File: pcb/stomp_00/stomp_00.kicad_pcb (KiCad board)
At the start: 2 copper layers, 50 x 60 mm, 21 parts, among them J1 9V_Power_Input, J5 Conn_01x08_Pin, J6 Conn_01x08_Pin, J7 Conn_01x08_Pin, U4 XL1509-5.0, U5 AP7333-33SRG, U6 74HC595, U7 74HC165, U8 74HC4051, U9 SGTL5000XNAA3

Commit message: taking shape...
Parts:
- moved H1 81.6 mm to (87.0, -24.0)
- moved H2 81.6 mm to (117.0, -24.0)
- moved H3 81.6 mm to (80.0, 30.0)
- moved H4 81.6 mm to (124.0, 30.0)
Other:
- board size 50 x 60 mm -> 56 x 65 mm
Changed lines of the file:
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@@
   )
   (footprint "MountingHole:MountingHole_3.2mm_M3" (layer "F.Cu")
-    (at 3 57)
+    (at 80 30)
     (descr "Mounting Hole 3.2mm, no annular, M3")
     (tags "mounting hole 3.2mm no annular m3")
@@
   )
   (footprint "MountingHole:MountingHole_3.2mm_M3" (layer "F.Cu")
-    (at 40 3)
+    (at 117 -24)
     (descr "Mounting Hole 3.2mm, no annular, M3")
     (tags "mounting hole 3.2mm no annular m3")
@@
   )
   (footprint "MountingHole:MountingHole_3.2mm_M3" (layer "F.Cu")
-    (at 47 57)
+    (at 124 30)
     (descr "Mounting Hole 3.2mm, no annular, M3")
     (tags "mounting hole 3.2mm no annular m3")
@@
   )
   (footprint "MountingHole:MountingHole_3.2mm_M3" (layer "F.Cu")
-    (at 10 3)
+    (at 87 -24)
     (descr "Mounting Hole 3.2mm, no annular, M3")
     (tags "mounting hole 3.2mm no annular m3")
@@
     )
   )
-  (gr_rect (start 16 22) (end 34 60)
-    (stroke (width 0.15) (type default)) (fill none) (layer "Dwgs.User"))
-  (gr_rect (start 0 35) (end 50 60)
-    (stroke (width 0.15) (type default)) (fill none) (layer "Dwgs.User"))
-  (gr_line (start 50 8) (end 50 60)
+  (gr_line (start 56 8) (end 56 65)
     (stroke (width 0.1) (type default)) (layer "Edge.Cuts"))
-  (gr_line (start 50 60) (end 0 60)
+  (gr_line (start 56 65) (end 0 65)
     (stroke (width 0.1) (type default)) (layer "Edge.Cuts"))
-  (gr_line (start 8 0) (end 42 0)
+  (gr_line (start 8 0) (end 48 0)
     (stroke (width 0.1) (type default)) (layer "Edge.Cuts"))
   (gr_arc (start 8 0) (mid 5.656854 5.656854) (end 0 8)
     (stroke (width 0.1) (type default)) (layer "Edge.Cuts"))
-  (gr_line (start 0 60) (end 0 8)
+  (gr_line (start 0 65) (end 0 8)
     (stroke (width 0.1) (type default)) (layer "Edge.Cuts"))
-  (gr_arc (start 50 8) (mid 44.343146 5.656854) (end 42 0)
+  (gr_arc (start 56 8) (mid 50.343146 5.656854) (end 48 0)
     (stroke (width 0.1) (type default)) (layer "Edge.Cuts"))
 )

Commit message: teensy footprint
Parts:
- removed U8: 74HC4051, Package_SO:SOIC-16_3.9x9.9mm_P1.27mm
- added D3: 1N4148, Diode_SMD:D_SOD-123, F.Cu at (194.2, 68.7)
- added J10: AudioJack3, Connector_PinHeader_2.54mm:PinHeader_1x03_P2.54mm_Vertical, F.Cu at (184.3, 69.4)
- added J11: AudioJack3, Connector_PinHeader_2.54mm:PinHeader_1x03_P2.54mm_Vertical, F.Cu at (188.9, 69.4)
- added R1: 2.2k, Resistor_SMD:R_0603_1608Metric, F.Cu at (201.0, 73.5)
- added R10: R_US, Resistor_SMD:R_0603_1608Metric, F.Cu at (198.8, 44.2)
- added R11: R_US, Resistor_SMD:R_0603_1608Metric, F.Cu at (198.8, 46.7)
- added R17: 220R, Resistor_SMD:R_0603_1608Metric, F.Cu at (179.9, 56.6)
- added R18: 10k, Resistor_SMD:R_0603_1608Metric, F.Cu at (179.9, 59.1)
- added R19: 47R, Resistor_SMD:R_0603_1608Metric, F.Cu at (179.9, 61.6)
- added R2: 2.2k, Resistor_SMD:R_0603_1608Metric, F.Cu at (201.0, 76.0)
- added R20: 47R, Resistor_SMD:R_0603_1608Metric, F.Cu at (179.9, 64.1)
- added R21: 470R, Resistor_SMD:R_0603_1608Metric, F.Cu at (179.9, 66.6)
- added R3: 100, Resistor_SMD:R_0603_1608Metric, F.Cu at (201.0, 78.5)
- added R4: R_US, Resistor_SMD:R_0603_1608Metric, F.Cu at (198.8, 29.1)
- added R5: R_US, Resistor_SMD:R_0603_1608Metric, F.Cu at (198.8, 31.6)
- added R6: R_US, Resistor_SMD:R_0603_1608Metric, F.Cu at (198.8, 34.1)
- added R7: R_US, Resistor_SMD:R_0603_1608Metric, F.Cu at (198.8, 36.6)
- added R8: R_US, Resistor_SMD:R_0603_1608Metric, F.Cu at (198.8, 39.1)
- added R9: R_US, Resistor_SMD:R_0603_1608Metric, F.Cu at (198.8, 41.6)
- added RV1: R_Potentiometer_US, Potentiometer_THT:Potentiometer_Piher_PC-16_Single_Vertical, F.Cu at (14.9, 28.6)
- added RV2: R_Potentiometer_US, Potentiometer_THT:Potentiometer_Piher_PC-16_Single_Vertical, F.Cu at (32.5, 28.6)
- added RV3: R_Potentiometer_US, Potentiometer_THT:Potentiometer_Piher_PC-16_Single_Vertical, F.Cu at (50.0, 28.6)
- added SW1: SW_DIP_x04, Button_Switch_THT:SW_DIP_SPSTx04_Slide_9.78x12.34mm_W7.62mm_P2.54mm, F.Cu at (179.9, 42.5)
- added U1: 4051, Package_SO:SOIC-16_3.9x9.9mm_P1.27mm, F.Cu at (163.3, 33.6)
- added U11: 74HC165, Package_SO:SOIC-16_3.9x9.9mm_P1.27mm, F.Cu at (182.2, 33.6)
- added U12: 74HC595, Package_SO:SOIC-16_3.9x9.9mm_P1.27mm, F.Cu at (205.1, 33.6)
- added U13: 74HC165, Package_SO:SOIC-16_3.9x9.9mm_P1.27mm, F.Cu at (190.6, 33.6)
- added U14: 6N138, Package_DIP:PowerIntegrations_SMD-8, F.Cu at (188.0, 61.2)
- added U2: TL072, Package_SO:SOIC-8_3.9x4.9mm_P1.27mm, F.Cu at (203.3, 58.6)
- added U3: TL072, Package_SO:SOIC-8_3.9x4.9mm_P1.27mm, F.Cu at (203.3, 67.0)
- U6: value 74HC595 -> 4051
- U7: value 74HC165 -> Teensy4.1; footprint Package_SO:SOIC-16_3.9x9.9mm_P1.27mm -> teensy:Teensy41; moved to B.Cu
- moved J5 94.1 mm to (94.0, -5.62)
- moved U6 79.0 mm to (171.7, 33.6)
- moved U7 76.9 mm to (28.2, 32.2), turned to -90 degrees
- moved J7 75.8 mm to (81.0, 3.12)
- moved J6 49.0 mm to (97.0, 14.9)

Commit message: seeing whether everything will fit...
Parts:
- removed J7: Conn_01x08_Pin, Connector_PinHeader_2.54mm:PinHeader_1x08_P2.54mm_Vertical
- removed R10, R11, R4, R5, R6, R7, R8, R9: R_US, Resistor_SMD:R_0603_1608Metric
- removed RV1, RV2, RV3: R_Potentiometer_US, Potentiometer_THT:Potentiometer_Piher_PC-16_Single_Vertical
- removed U1, U6: 4051, Package_SO:SOIC-16_3.9x9.9mm_P1.27mm
- removed U11, U13: 74HC165, Package_SO:SOIC-16_3.9x9.9mm_P1.27mm
- removed U12: 74HC595, Package_SO:SOIC-16_3.9x9.9mm_P1.27mm
- added J4: Headphones, Connector_PinHeader_2.54mm:PinHeader_1x03_P2.54mm_Vertical, F.Cu at (90.2, 19.1)
- added J9: Conn_01x04_Pin, Connector_PinHeader_2.54mm:PinHeader_1x04_P2.54mm_Vertical, F.Cu at (167.8, 5.53)
- added RV4: R_Potentiometer_US, Potentiometer_THT:Potentiometer_Piher_PC-16_Single_Vertical, F.Cu at (15.6, 29.0)
- added RV5: R_Potentiometer_US, Potentiometer_THT:Potentiometer_Piher_PC-16_Single_Vertical, F.Cu at (33.2, 29.0)
- added RV6: R_Potentiometer_US, Potentiometer_THT:Potentiometer_Piher_PC-16_Single_Vertical, F.Cu at (50.7, 29.0)
- J1: footprint Connector_BarrelJack:BarrelJack_Horizontal -> Connector_PinHeader_2.54mm:PinHeader_1x03_P2.54mm_Vertical
- J5, J6: value Conn_01x08_Pin -> Conn_01x24_Pin; footprint Connector_PinHeader_2.54mm:PinHeader_1x08_P2.54mm_Vertical -> Connector_PinHeader_2.54mm:PinHeader_1x24_P2.54mm_Vertical
- SW1: moved to B.Cu
- moved SW1 131.9 mm to (50.8, 15.2), turned to 180 degrees
- moved C3 99.8 mm to (3.81, 58.4)
- moved J1 97.5 mm to (8.89, 7.62), turned to 90 degrees
- moved L1 96.7 mm to (3.81, 35.6)
- moved C5 85.0 mm to (3.81, 45.7)
- moved J5 76.8 mm to (17.8, 3.81)
- moved D2 72.7 mm to (12.7, 52.1), turned to 90 degrees
- moved J6 59.9 mm to (38.1, 3.81)
- moved U7 0.82 mm to (27.9, 33.0)
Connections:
- U7 pad 10: unconnected-(U7-8_TX2_IN1-Pad10) -> DAC_DOUT
- U7 pad 2: unconnected-(U7-0_RX1_CRX2_CS1-Pad2) -> MIDI_IN
- U7 pad 3: unconnected-(U7-1_TX1_CTX2_MISO1-Pad3) -> MIDI_OUT
- U7 pad 40: unconnected-(U7-18_A4_SDA-Pad40) -> DAC_SDA
- U7 pad 41: unconnected-(U7-19_A5_SCL-Pad41) -> DAC_SCL
- U7 pad 42: unconnected-(U7-20_A6_TX5_LRCLK1-Pad42) -> DAC_LRCLK
- U7 pad 43: unconnected-(U7-21_A7_RX5_BCLK1-Pad43) -> DAC_BCLK
- U7 pad 45: unconnected-(U7-23_A9_CRX1_MCLK1-Pad45) -> DAC_MCLK
- U7 pad 9: unconnected-(U7-7_RX2_OUT1A-Pad9) -> DAC_DIN

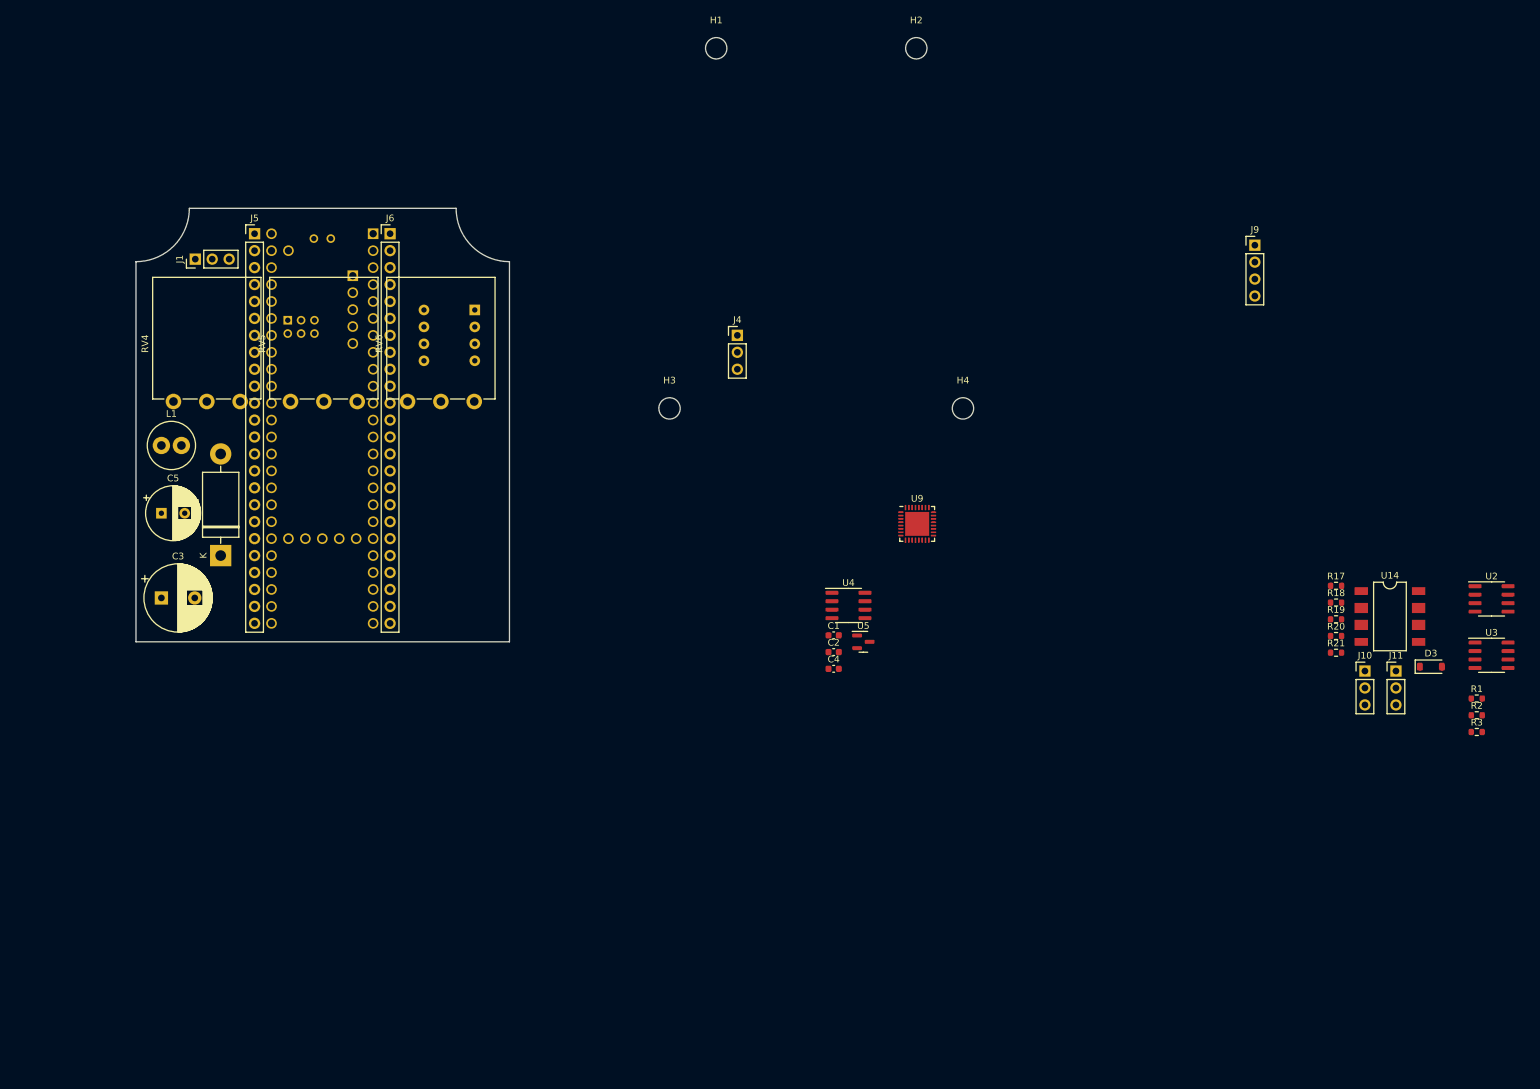
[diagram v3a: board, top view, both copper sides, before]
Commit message: input stage schematic
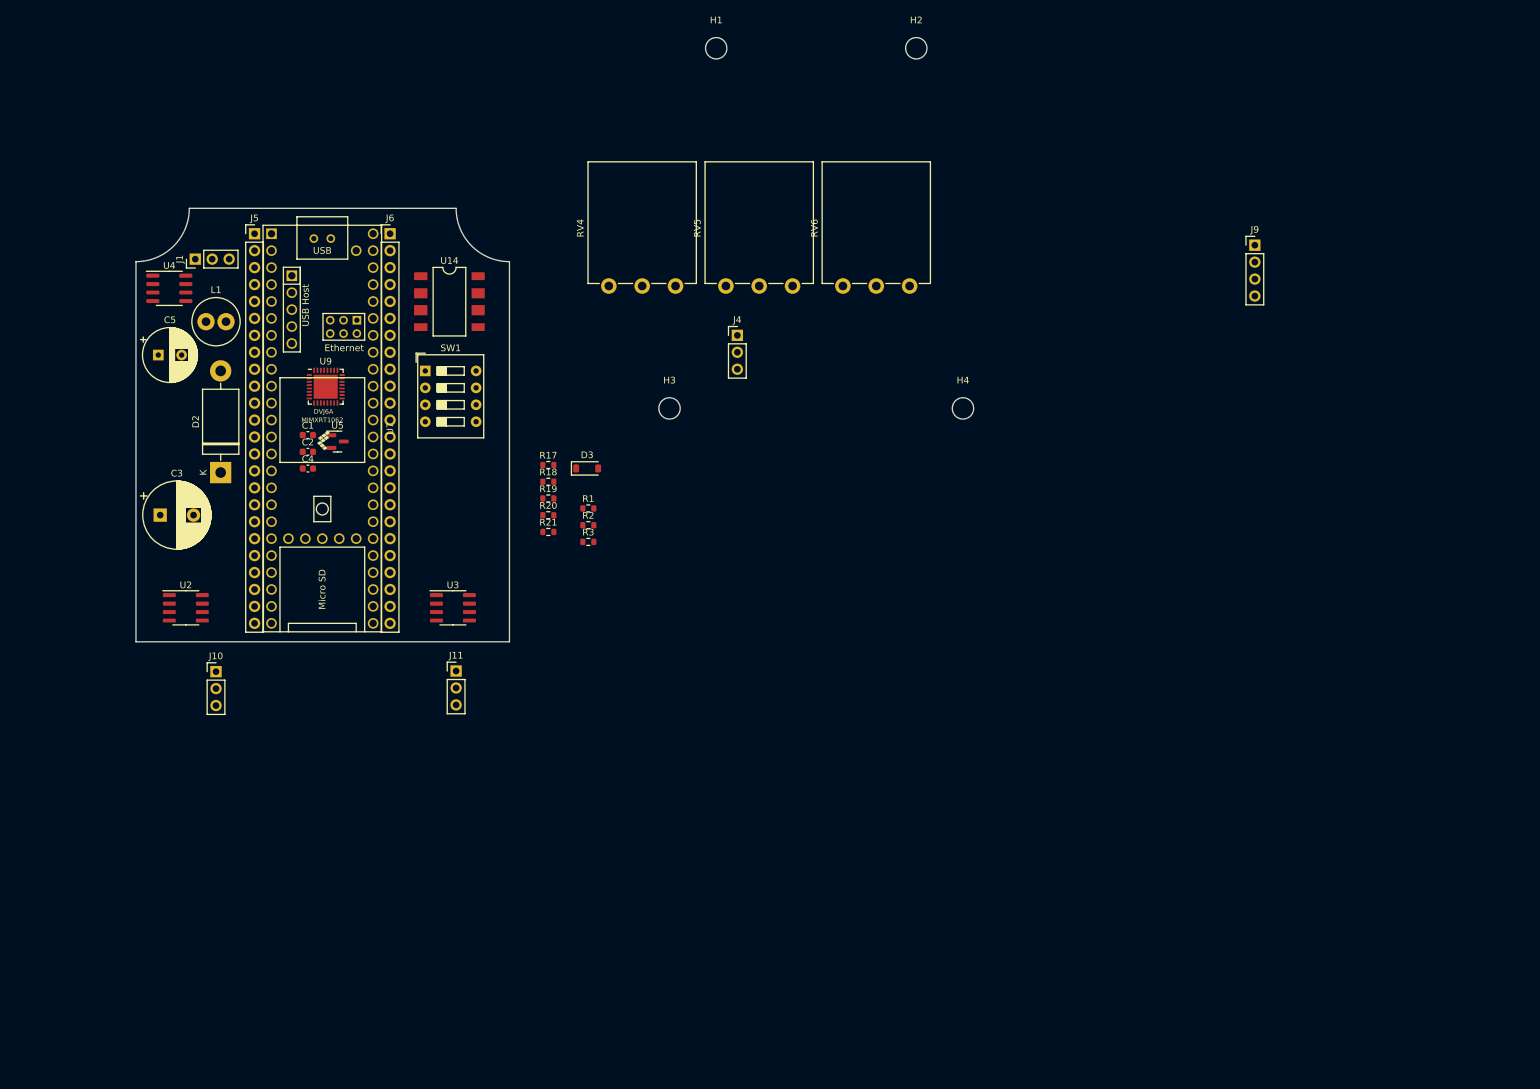
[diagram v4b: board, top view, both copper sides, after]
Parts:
- SW1, U7: moved to F.Cu
- moved U2 195.8 mm to (7.47, 59.9)
- moved J10 172.3 mm to (12.0, 69.5)
- moved U3 155.9 mm to (47.5, 59.9)
- moved U14 148.7 mm to (47.0, 14.0)
- moved J11 140.9 mm to (48.0, 69.4)
- moved R1 136.2 mm to (67.8, 45.0)
- moved R2 136.2 mm to (67.8, 47.5)
- moved R3 136.2 mm to (67.8, 50.0)
- moved D3 130.0 mm to (67.7, 39.0)
- moved R17 119.5 mm to (61.8, 38.5)
- moved R18 119.5 mm to (61.8, 41.0)
- moved R19 119.5 mm to (61.8, 43.5)
- moved R20 119.5 mm to (61.8, 46.0)
- moved R21 119.5 mm to (61.8, 48.5)
- moved U4 112.4 mm to (5.00, 12.0)
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
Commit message: better layout in enclosure
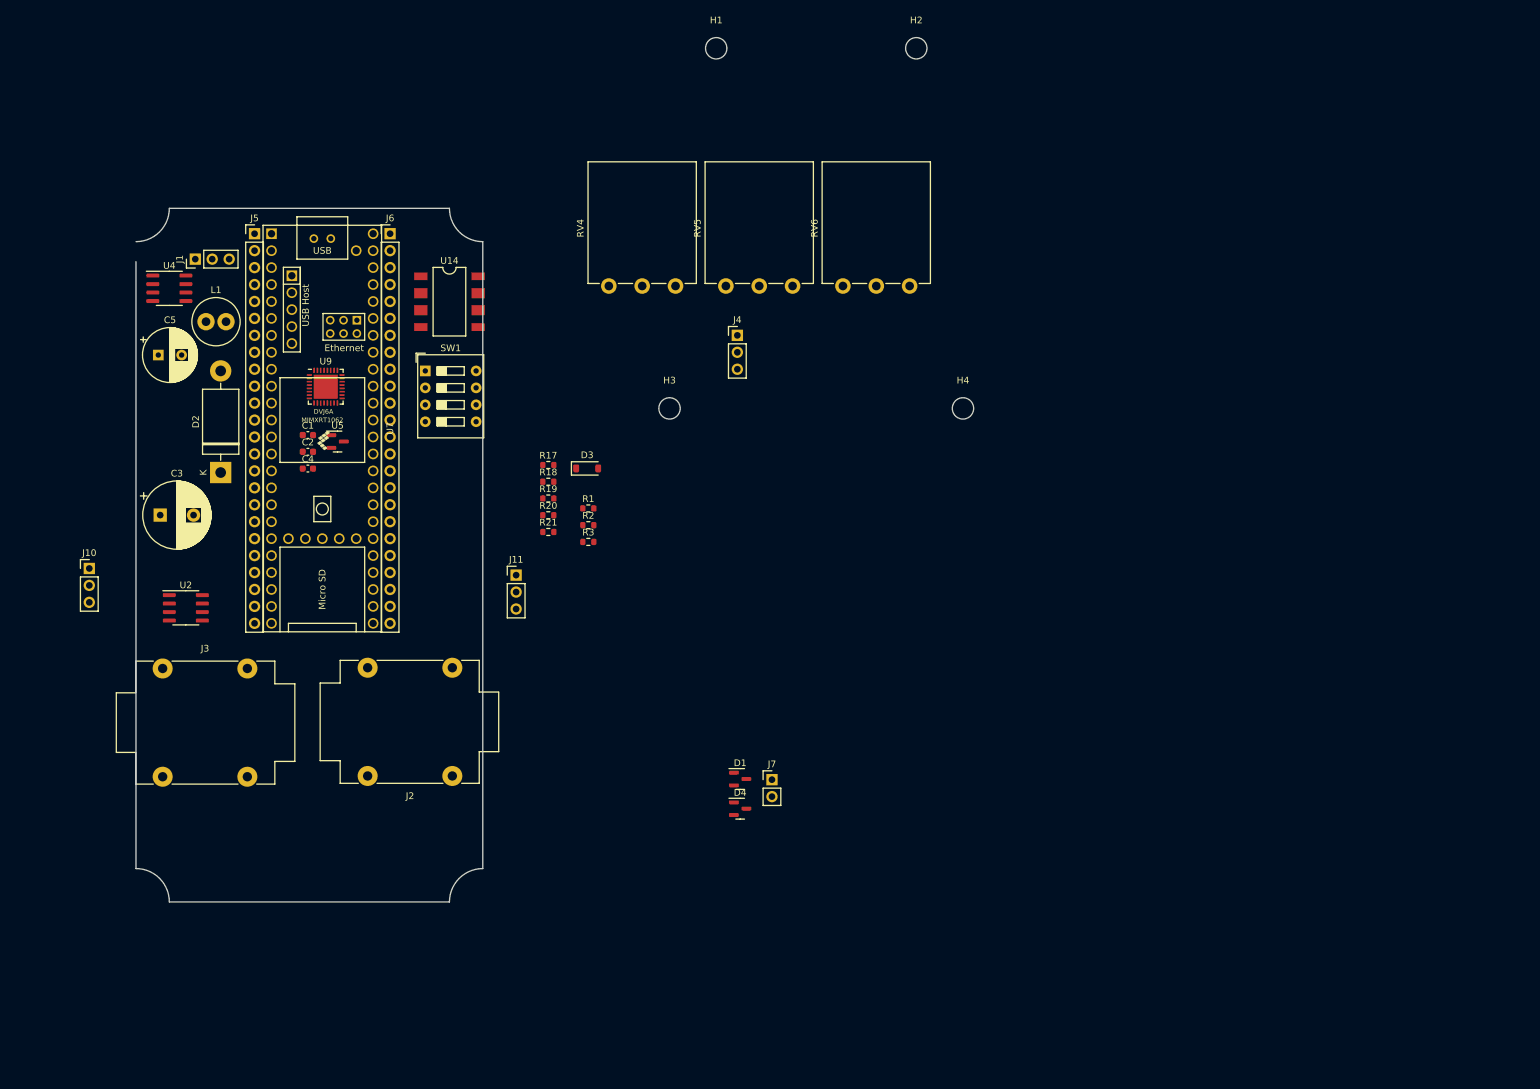
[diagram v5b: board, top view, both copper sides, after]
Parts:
- removed J9: Conn_01x04_Pin, Connector_PinHeader_2.54mm:PinHeader_1x04_P2.54mm_Vertical
- removed U3: TL072, Package_SO:SOIC-8_3.9x4.9mm_P1.27mm
- added D1: BAT54S, Package_TO_SOT_SMD:SOT-23, F.Cu at (90.6, 85.6)
- added D4: BAT54S, Package_TO_SOT_SMD:SOT-23, F.Cu at (90.6, 90.0)
- added J2: GuitarInput1, Connector_Audio:Jack_6.35mm_Neutrik_NMJ4HCD2_Horizontal, F.Cu at (47.4, 85.1)
- added J3: GuitarOutput1, Connector_Audio:Jack_6.35mm_Neutrik_NMJ4HCD2_Horizontal, F.Cu at (4.00, 69.0)
- added J7: GuitarInput2, Connector_PinHeader_2.54mm:PinHeader_1x02_P2.54mm_Vertical, F.Cu at (95.4, 85.7)
- moved J10 24.5 mm to (-7.00, 54.0)
- moved J11 17.0 mm to (57.0, 55.0)
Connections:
- net LINE_IN_L renamed Net-(U9-LINEIN_L)
- net LINE_IN_R renamed Net-(U9-LINEIN_R)
- U2 pad 1: unconnected-(U2-Pad1) -> Net-(C10-Pad2)
- U2 pad 2: unconnected-(U2A---Pad2) -> Net-(U2A--)
- U2 pad 3: unconnected-(U2A-+-Pad3) -> Net-(U2A-+)
- U2 pad 4: unconnected-(U2C-V--Pad4) -> GNDA
- U2 pad 5: unconnected-(U2B-+-Pad5) -> Net-(U2B-+)
- U2 pad 6: unconnected-(U2B---Pad6) -> Net-(U2B--)
- U2 pad 7: unconnected-(U2-Pad7) -> Net-(C15-Pad2)
- U2 pad 8: unconnected-(U2C-V+-Pad8) -> +9V
- U9 pad 11: unconnected-(U9-LINEOUT_R-Pad11) -> Net-(U9-LINEOUT_R)
- U9 pad 12: unconnected-(U9-LINEOUT_L-Pad12) -> Net-(U9-LINEOUT_L)
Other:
- board size 56 x 65 mm -> 52 x 104 mm

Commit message: good progress with physical layout
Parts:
- removed J5, J6: Conn_01x24_Pin, Connector_PinHeader_2.54mm:PinHeader_1x24_P2.54mm_Vertical
- added J8: Conn_01x09_Pin, Connector_PinHeader_2.54mm:PinHeader_1x09_P2.54mm_Vertical, F.Cu at (-17.0, 73.8)
- added SW2: SW_3PDT, stomp:Footswitch_3PDT, F.Cu at (21.0, 91.4)
- U7: footprint teensy:Teensy41 -> stomp:Teensy41_stomp
- moved J3 4.47 mm to (6.00, 65.0)
- moved J2 3.89 mm to (47.7, 81.2)
- moved U7 1.84 mm to (27.6, 31.2)
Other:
- board size 52 x 104 mm -> 54 x 106 mm
